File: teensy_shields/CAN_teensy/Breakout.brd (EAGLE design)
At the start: 39.4 x 20.3 mm, 4 parts, among them IC1 SN65HVD230D

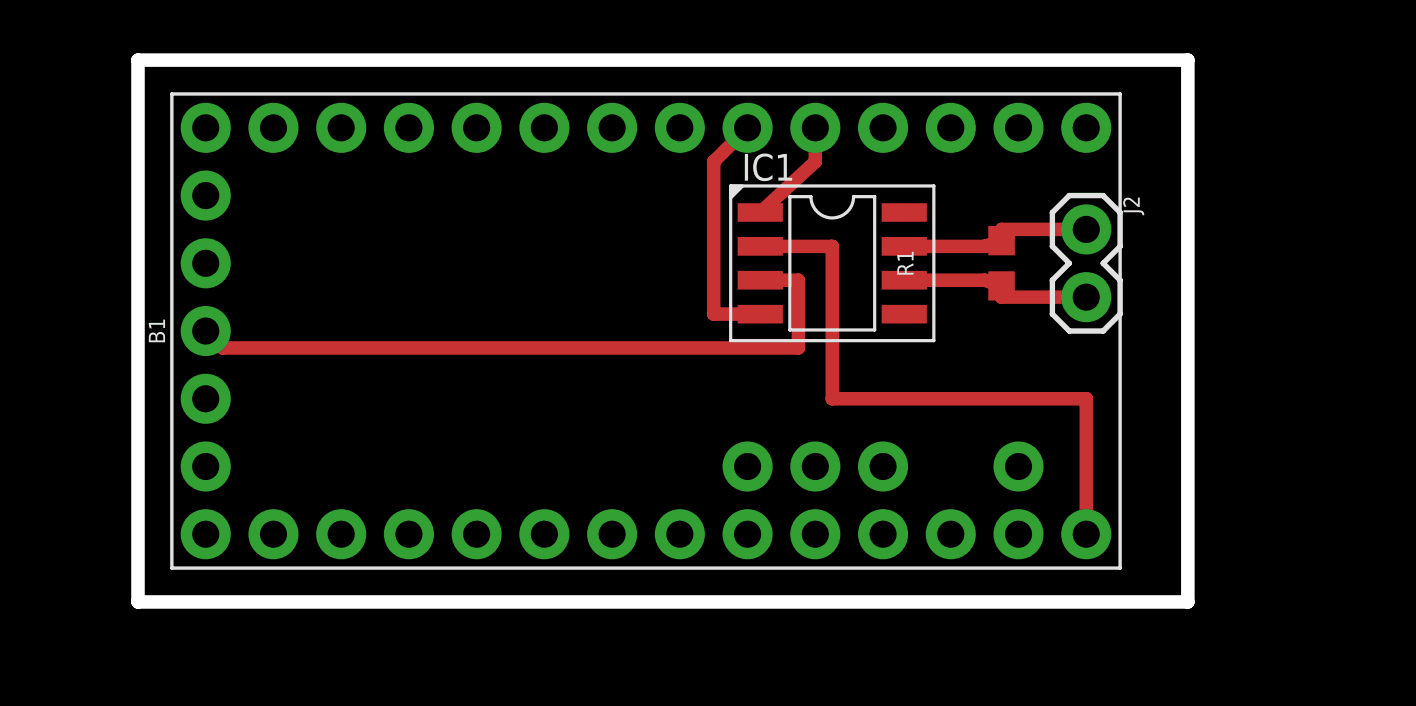
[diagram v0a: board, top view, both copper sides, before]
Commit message: updated CAN shield
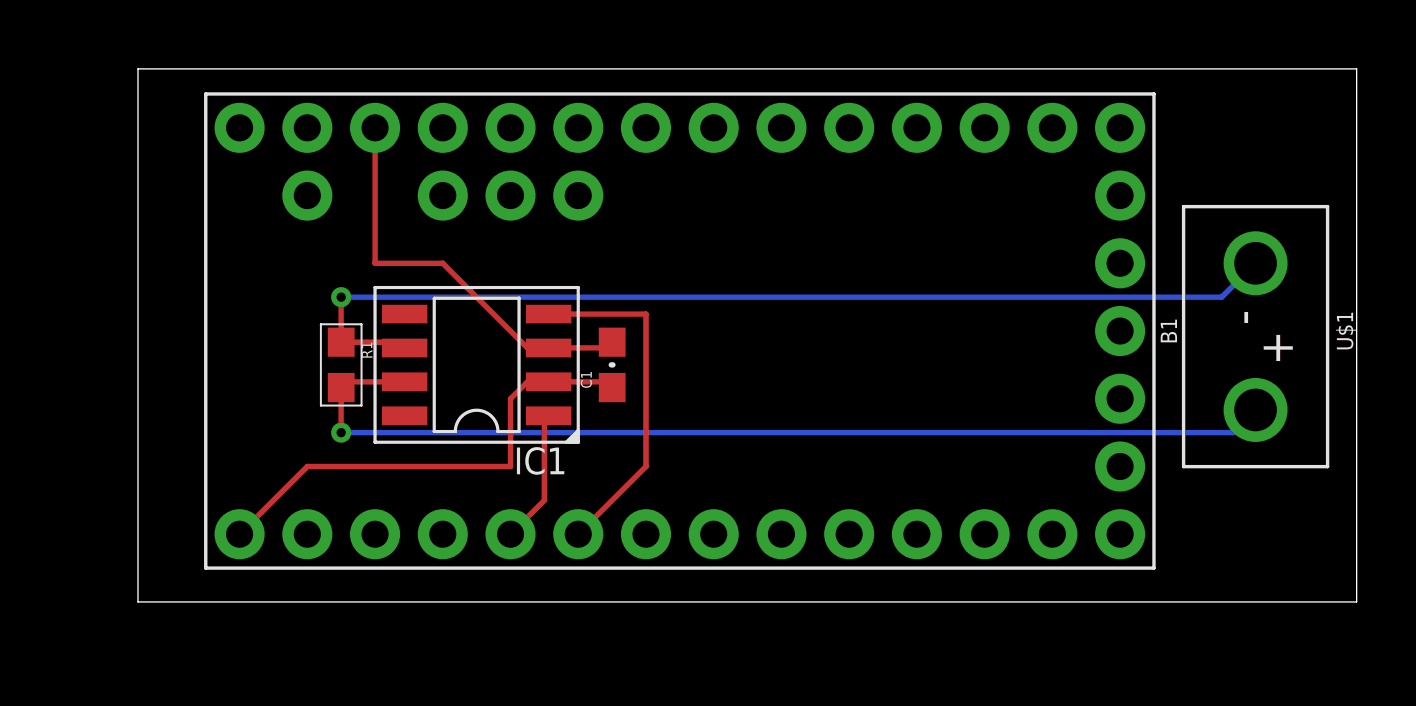
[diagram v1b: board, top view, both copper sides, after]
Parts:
- removed J2: (no value), SparkFun-Connectors:1X02
- added C1: (no value), SparkFun-Capacitors:0603-CAP
- added U$1: HEADER2, Custom_old:2PINVALULOK
- added U$2: DEV, Custom_old:DEV
- R1: value 1.8M -> (none); device SparkFun-Resistors:0603 -> SparkFun-Passives:0603-RES
- moved R1 25.1 mm to (7.62, 8.89), turned to 270 degrees
- moved IC1 13.9 mm to (12.7, 8.89), turned to 180 degrees
- moved B1 1.27 mm to (20.3, 10.2), turned to 270 degrees
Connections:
- removed net 3.3V: B1.3.3V
- removed net 5V: B1.VIN, IC1.2
- removed net GND: B1.GND, IC1.3
- removed net N$5: IC1.6, J2.2, R1.1
- removed net N$6: IC1.7, J2.1, R1.2
- new net CANH: IC1.7, R1.2, U$1.1
- new net CANL: IC1.6, R1.1, U$1.2
- new net VIN: B1.VIN
- net 3V: now also B1.3.3V, C1.2, IC1.3
- net GND1: now also B1.GND, C1.1, IC1.2
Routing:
- net CANL: track 0.00 -> 39.0 mm, vias 0 -> 1
- net CANH: track 0.00 -> 38.8 mm, vias 0 -> 1
- net GND: track 26.5 -> 0.00 mm
- net 5V: track 23.0 -> 0.00 mm
- net GND1: track 0.00 -> 17.9 mm
- net 3V: track 0.00 -> 15.4 mm
- net N$6: track 7.28 -> 0.00 mm
- net N$5: track 7.28 -> 0.00 mm
- net N$2: track 9.26 -> 13.0 mm
- net N$1: track 4.08 -> 5.04 mm
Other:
- board size 39.4 x 20.3 mm -> 45.7 x 20 mm

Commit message: cleanup
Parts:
- R1: value (none) -> 120
- moved U$2 21.1 mm to (19.1, 6.35)
- moved C1 2.84 mm to (15.2, 7.62)
- moved R1 2.84 mm to (5.08, 7.62)
- moved IC1 2.84 mm to (10.2, 7.62)
- moved B1 2.84 mm to (17.8, 8.89)
- moved U$1 2.84 mm to (39.4, 11.4)
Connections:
- removed net AGND: B1.AGND
- removed net GND1: B1.GND, B1.GND1, C1.1, IC1.2
- new net EN_CAN: B1.2, IC1.8
- new net GND: B1.AGND, B1.GND, B1.GND1, C1.1, IC1.2
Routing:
- net GND1: track 17.9 -> 0.00 mm
- net EN_CAN: track 0.00 -> 5.04 mm
- net GND: track 0.00 -> 2.47 mm
- added copper zone on layer 1, net GND
- added copper zone on layer 16, net GND
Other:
- board size 45.7 x 20 mm -> 43.3 x 18 mm
- board text added: "CAN shield v1.0 Nov. 6, 2018 Designed by Nate Mela"
- board text added: "CANH"
- board text added: "CANL"

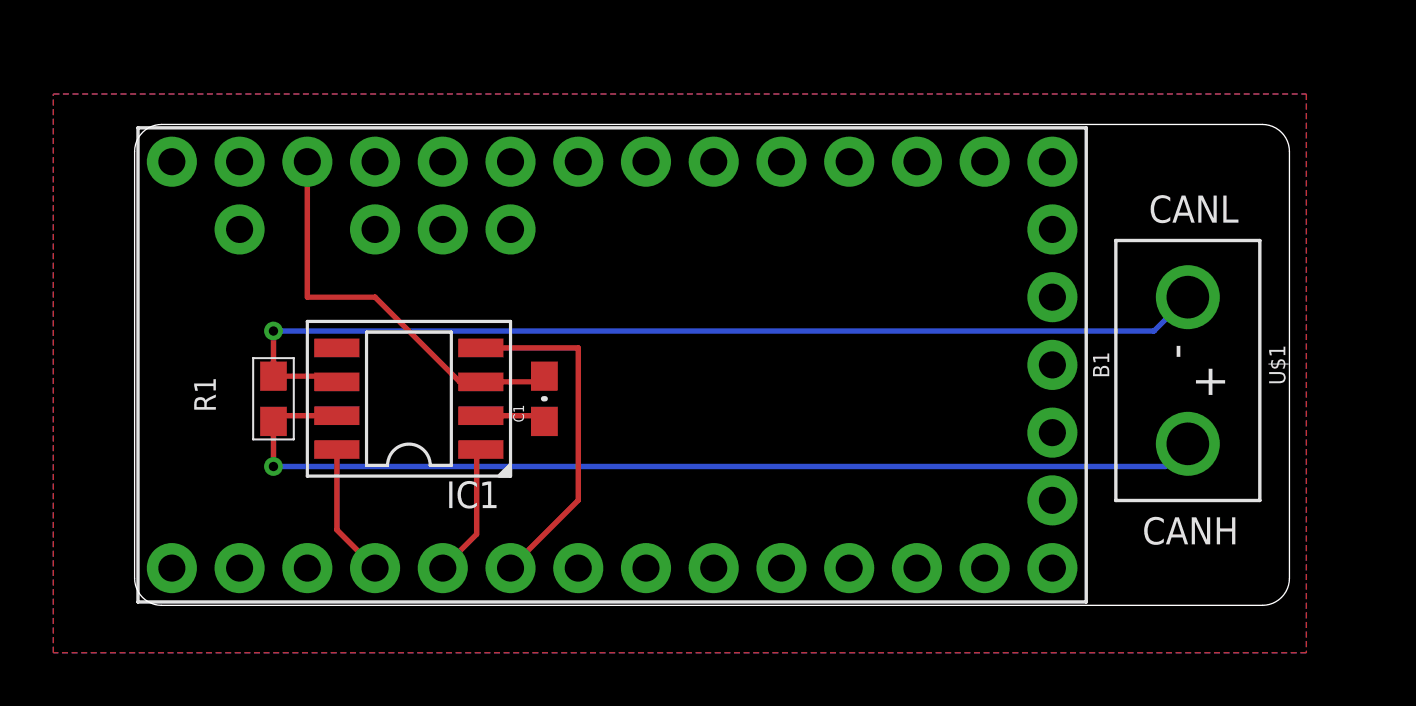
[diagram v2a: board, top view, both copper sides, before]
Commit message: final boards sent to JLCPCB
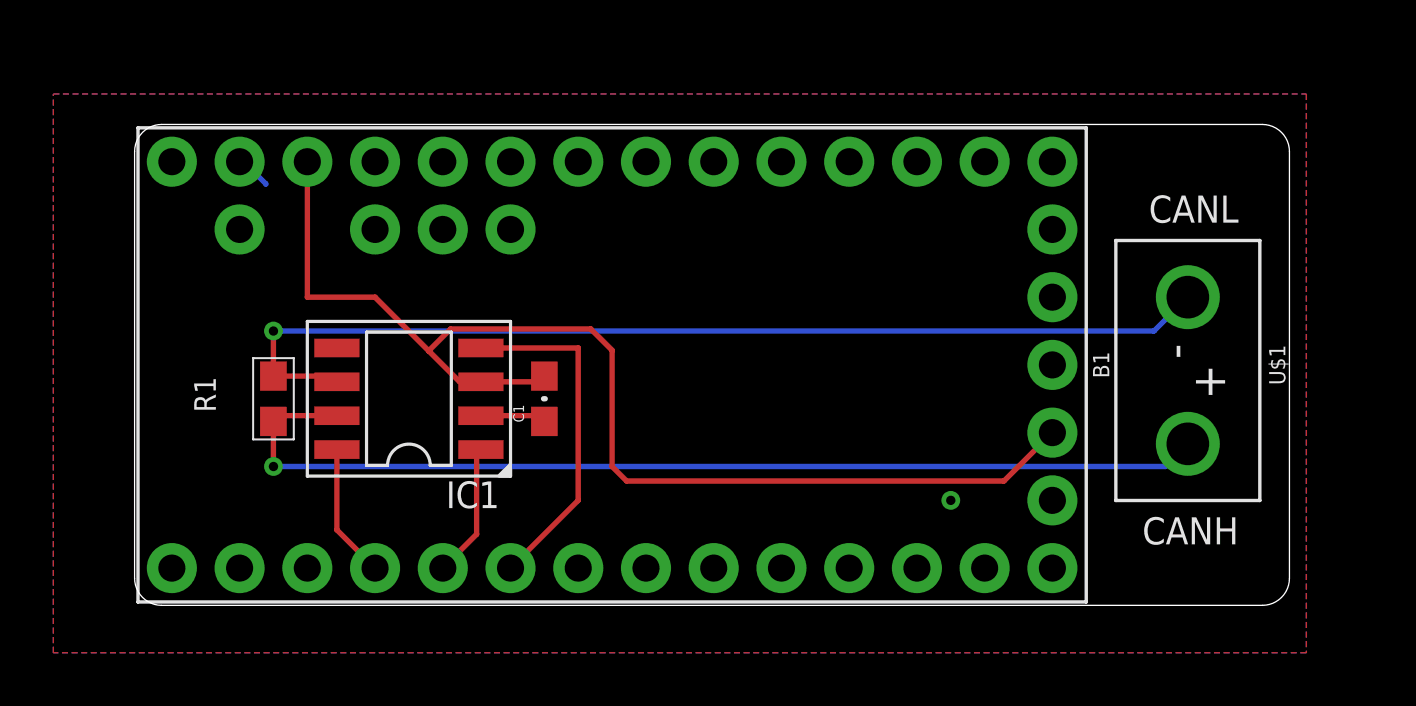
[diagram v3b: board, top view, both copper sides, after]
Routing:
- net 3V: track 15.4 -> 44.8 mm
- net GND: track 2.47 -> 3.81 mm, vias 0 -> 1
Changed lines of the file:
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@@
 <layer number="14" name="Route14" color="22" fill="1" visible="no" active="no"/>
 <layer number="15" name="Route15" color="23" fill="1" visible="no" active="no"/>
-<layer number="16" name="Bottom" color="1" fill="1" visible="yes" active="yes"/>
+<layer number="16" name="Bottom" color="1" fill="1" visible="no" active="yes"/>
 <layer number="17" name="Pads" color="2" fill="1" visible="yes" active="yes"/>
 <layer number="18" name="Vias" color="2" fill="1" visible="yes" active="yes"/>
@@
 <layer number="20" name="Dimension" color="24" fill="1" visible="yes" active="yes"/>
 <layer number="21" name="tPlace" color="7" fill="1" visible="yes" active="yes"/>
-<layer number="22" name="bPlace" color="7" fill="1" visible="yes" active="yes"/>
+<layer number="22" name="bPlace" color="7" fill="1" visible="no" active="yes"/>
 <layer number="23" name="tOrigins" color="15" fill="1" visible="yes" active="yes"/>
-<layer number="24" name="bOrigins" color="15" fill="1" visible="yes" active="yes"/>
+<layer number="24" name="bOrigins" color="15" fill="1" visible="no" active="yes"/>
 <layer number="25" name="tNames" color="7" fill="1" visible="yes" active="yes"/>
-<layer number="26" name="bNames" color="7" fill="1" visible="yes" active="yes"/>
-<layer number="27" name="tValues" color="7" fill="1" visible="yes" active="yes"/>
-<layer number="28" name="bValues" color="7" fill="1" visible="yes" active="yes"/>
-<layer number="29" name="tStop" color="7" fill="3" visible="no" active="yes"/>
+<layer number="26" name="bNames" color="7" fill="1" visible="no" active="yes"/>
+<layer number="27" name="tValues" color="7" fill="1" visible="no" active="yes"/>
+<layer number="28" name="bValues" color="7" fill="1" visible="no" active="yes"/>
+<layer number="29" name="tStop" color="7" fill="3" visible="yes" active="yes"/>
 <layer number="30" name="bStop" color="7" fill="6" visible="no" active="yes"/>
 <layer number="31" name="tCream" color="7" fill="4" visible="no" active="yes"/>
@@
 <layer number="38" name="bTest" color="7" fill="1" visible="no" active="yes"/>
 <layer number="39" name="tKeepout" color="4" fill="11" visible="yes" active="yes"/>
-<layer number="40" name="bKeepout" color="1" fill="11" visible="yes" active="yes"/>
+<layer number="40" name="bKeepout" color="1" fill="11" visible="no" active="yes"/>
 <layer number="41" name="tRestrict" color="4" fill="10" visible="yes" active="yes"/>
-<layer number="42" name="bRestrict" color="1" fill="10" visible="yes" active="yes"/>
+<layer number="42" name="bRestrict" color="1" fill="10" visible="no" active="yes"/>
 <layer number="43" name="vRestrict" color="2" fill="10" visible="no" active="yes"/>
-<layer number="44" name="Drills" color="7" fill="1" visible="yes" active="yes"/>
+<layer number="44" name="Drills" color="7" fill="1" visible="no" active="yes"/>
 <layer number="45" name="Holes" color="7" fill="1" visible="yes" active="yes"/>
 <layer number="46" name="Milling" color="3" fill="1" visible="no" active="yes"/>
@@
 <layer number="49" name="Reference" color="7" fill="1" visible="no" active="yes"/>
 <layer number="50" name="dxf" color="7" fill="1" visible="no" active="no"/>
-<layer number="51" name="tDocu" color="7" fill="1" visible="no" active="yes"/>
+<layer number="51" name="tDocu" color="7" fill="1" visible="yes" active="yes"/>
 <layer number="52" name="bDocu" color="7" fill="1" visible="no" active="yes"/>
 <layer number="53" name="tGND_GNDA" color="7" fill="9" visible="no" active="no"/>
@@
 <wire x1="8.89" y1="11.43" x2="6.35" y2="11.43" width="0.2032" layer="1"/>
 <wire x1="6.35" y1="11.43" x2="6.35" y2="16.51" width="0.2032" layer="1"/>
-<wire x1="12.065" y1="8.255" x2="8.89" y2="11.43" width="0.2032" layer="1"/>
-<wire x1="15.24" y1="8.47" x2="34.29" y2="6.35" width="0" layer="19" extent="1-1"/>
+<wire x1="12.065" y1="8.255" x2="10.90295" y2="9.41705" width="0.2032" layer="1"/>
+<wire x1="10.90295" y1="9.41705" x2="8.89" y2="11.43" width="0.2032" layer="1"/>
+<wire x1="11.7221" y1="10.2362" x2="16.9799" y2="10.2362" width="0.2032" layer="1"/>
+<wire x1="10.8966" y1="9.4107" x2="10.90295" y2="9.41705" width="0.2032" layer="1"/>
+<wire x1="10.90295" y1="9.41705" x2="11.7221" y2="10.2362" width="0.2032" layer="1"/>
+<wire x1="10.8966" y1="9.4107" x2="10.90295" y2="9.41705" width="0.2032" layer="1"/>
+<wire x1="32.4739" y1="4.5339" x2="34.29" y2="6.35" width="0.2032" layer="1"/>
+<wire x1="16.9799" y1="10.2362" x2="17.78" y2="9.4361" width="0.2032" layer="1"/>
+<wire x1="17.78" y1="9.4361" x2="17.78" y2="5.08" width="0.2032" layer="1"/>
+<wire x1="17.78" y1="5.08" x2="18.3261" y2="4.5339" width="0.2032" layer="1"/>
+<wire x1="18.3261" y1="4.5339" x2="32.4739" y2="4.5339" width="0.2032" layer="1"/>
 </signal>
 <signal name="VIN">
@@
 <wire x1="12.86" y1="6.985" x2="15.025" y2="6.985" width="0.2032" layer="1"/>
 <wire x1="15.025" y1="6.985" x2="15.24" y2="6.77" width="0.2032" layer="1"/>
-<wire x1="12.86" y1="6.985" x2="3.81" y2="16.51" width="0" layer="19" extent="1-1"/>
+<wire x1="4.7879" y1="15.6845" x2="3.9624" y2="16.51" width="0.2032" layer="16"/>
+<wire x1="3.9624" y1="16.51" x2="3.81" y2="16.51" width="0.2032" layer="16"/>
+<wire x1="4.7879" y1="15.6845" x2="4.798071875" y2="15.666103125" width="0.2032" layer="16"/>
+<via x="30.48" y="3.81" extent="1-16" drill="0.35"/>
 </signal>
 </signals>
